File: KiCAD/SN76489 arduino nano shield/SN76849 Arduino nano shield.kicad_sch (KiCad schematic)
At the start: 14 parts, among them J1 Arduino_in, J2 audio_debug, J3 OLED_wit, J5 LOGO, J6 gat1, J7 gat2, J8 geluid_uit, U1 PCF8574, U3 SN76489, X1 CLK_DIP14_4Mhz

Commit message: Bijgewerkt naar KiCAD 7.0
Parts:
- U1, U3: footprint w_pth_circuits:dil_16-300_socket -> Package_DIP:DIP-16_W7.62mm
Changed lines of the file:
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@@
     (effects (font (size 1.1176 1.1176)) (justify left bottom))
   )
-  (label "VSS" (at 112.268 66.04 0)
+  (label "VSS" (at 112.268 66.04 0) (fields_autoplaced)
     (effects (font (size 0.9144 0.9144)) (justify left bottom))
   )
-  (label "P1" (at 181.61 40.894 0)
+  (label "P1" (at 181.61 40.894 0) (fields_autoplaced)
     (effects (font (size 0.8128 0.8128)) (justify left bottom))
   )
-  (label "VCC" (at 115.57 27.178 90)
+  (label "VCC" (at 115.57 27.178 90) (fields_autoplaced)
     (effects (font (size 0.9144 0.9144)) (justify left bottom))
   )
-  (label "VCC" (at 181.356 28.194 0)
+  (label "VCC" (at 181.356 28.194 0) (fields_autoplaced)
     (effects (font (size 0.7112 0.7112)) (justify left bottom))
   )
-  (label "SDA" (at 146.304 65.786 0)
+  (label "SDA" (at 146.304 65.786 0) (fields_autoplaced)
     (effects (font (size 0.7112 0.7112)) (justify left bottom))
   )
-  (label "SDA" (at 93.98 37.592 0)
+  (label "SDA" (at 93.98 37.592 0) (fields_autoplaced)
     (effects (font (size 0.7112 0.7112)) (justify left bottom))
   )
-  (label "VSS" (at 208.534 113.792 180)
+  (label "VSS" (at 208.534 113.792 180) (fields_autoplaced)
     (effects (font (size 0.9144 0.9144)) (justify right bottom))
   )
-  (label "P3" (at 129.794 42.672 0)
+  (label "P3" (at 129.794 42.672 0) (fields_autoplaced)
     (effects (font (size 0.9144 0.9144)) (justify left bottom))
   )
-  (label "CE" (at 148.59 40.894 0)
+  (label "CE" (at 148.59 40.894 0) (fields_autoplaced)
     (effects (font (size 0.9144 0.9144)) (justify left bottom))
   )
-  (label "VSS" (at 80.772 78.486 0)
+  (label "VSS" (at 80.772 78.486 0) (fields_autoplaced)
     (effects (font (size 0.7112 0.7112)) (justify left bottom))
   )
-  (label "P0" (at 129.794 35.052 0)
+  (label "P0" (at 129.794 35.052 0) (fields_autoplaced)
     (effects (font (size 0.9144 0.9144)) (justify left bottom))
   )
-  (label "P6" (at 148.59 30.734 0)
+  (label "P6" (at 148.59 30.734 0) (fields_autoplaced)
     (effects (font (size 0.8128 0.8128)) (justify left bottom))
   )
-  (label "P2" (at 129.794 40.132 0)
+  (label "P2" (at 129.794 40.132 0) (fields_autoplaced)
     (effects (font (size 0.9144 0.9144)) (justify left bottom))
   )
-  (label "P7" (at 148.59 33.274 0)
+  (label "P7" (at 148.59 33.274 0) (fields_autoplaced)
     (effects (font (size 0.8128 0.8128)) (justify left bottom))
   )
-  (label "Clock" (at 80.264 67.818 0)
+  (label "Clock" (at 80.264 67.818 0) (fields_autoplaced)
     (effects (font (size 0.8128 0.8128)) (justify left bottom))
   )
-  (label "VSS" (at 146.05 79.248 180)
+  (label "VSS" (at 146.05 79.248 180) (fields_autoplaced)
     (effects (font (size 0.9144 0.9144)) (justify right bottom))
   )
-  (label "~{WE}" (at 148.59 38.354 0)
+  (label "~{WE}" (at 148.59 38.354 0) (fields_autoplaced)
     (effects (font (size 0.8128 0.8128)) (justify left bottom))
   )
-  (label "P4" (at 129.794 45.212 0)
+  (label "P4" (at 129.794 45.212 0) (fields_autoplaced)
     (effects (font (size 0.9144 0.9144)) (justify left bottom))
   )
-  (label "~{WE}" (at 80.772 51.054 0)
+  (label "~{WE}" (at 80.772 51.054 0) (fields_autoplaced)
     (effects (font (size 0.8128 0.8128)) (justify left bottom))
   )
-  (label "Clock" (at 181.61 33.274 0)
+  (label "Clock" (at 181.61 33.274 0) (fields_autoplaced)
     (effects (font (size 0.9144 0.9144)) (justify left bottom))
   )
-  (label "P4" (at 181.61 30.734 0)
+  (label "P4" (at 181.61 30.734 0) (fields_autoplaced)
     (effects (font (size 0.9144 0.9144)) (justify left bottom))
   )
-  (label "P0" (at 181.61 43.434 0)
+  (label "P0" (at 181.61 43.434 0) (fields_autoplaced)
     (effects (font (size 0.8128 0.8128)) (justify left bottom))
   )
-  (label "P5" (at 129.794 47.752 0)
+  (label "P5" (at 129.794 47.752 0) (fields_autoplaced)
     (effects (font (size 0.9144 0.9144)) (justify left bottom))
   )
-  (label "SDA" (at 80.772 48.514 0)
+  (label "SDA" (at 80.772 48.514 0) (fields_autoplaced)
     (effects (font (size 0.7112 0.7112)) (justify left bottom))
   )
-  (label "P1" (at 129.54 37.592 0)
+  (label "P1" (at 129.54 37.592 0) (fields_autoplaced)
     (effects (font (size 0.9144 0.9144)) (justify left bottom))
   )
-  (label "P2" (at 181.61 38.354 0)
+  (label "P2" (at 181.61 38.354 0) (fields_autoplaced)
     (effects (font (size 0.8128 0.8128)) (justify left bottom))
   )
-  (label "P6" (at 129.794 50.292 0)
+  (label "P6" (at 129.794 50.292 0) (fields_autoplaced)
     (effects (font (size 0.9144 0.9144)) (justify left bottom))
   )
-  (label "VSS" (at 148.59 45.974 0)
+  (label "VSS" (at 148.59 45.974 0) (fields_autoplaced)
     (effects (font (size 0.9144 0.9144)) (justify left bottom))
   )
-  (label "SCL" (at 94.234 35.052 0)
+  (label "SCL" (at 94.234 35.052 0) (fields_autoplaced)
     (effects (font (size 0.7112 0.7112)) (justify left bottom))
   )
-  (label "Audio" (at 146.812 94.996 180)
+  (label "Audio" (at 146.812 94.996 180) (fields_autoplaced)
     (effects (font (size 0.9144 0.9144)) (justify right bottom))
   )
-  (label "P7" (at 129.794 52.832 0)
+  (label "P7" (at 129.794 52.832 0) (fields_autoplaced)
     (effects (font (size 0.9144 0.9144)) (justify left bottom))
   )
-  (label "SCL" (at 80.772 45.974 0)
+  (label "SCL" (at 80.772 45.974 0) (fields_autoplaced)
     (effects (font (size 0.7112 0.7112)) (justify left bottom))
   )
-  (label "SCL" (at 146.304 63.246 0)
+  (label "SCL" (at 146.304 63.246 0) (fields_autoplaced)
     (effects (font (size 0.7112 0.7112)) (justify left bottom))
   )
-  (label "P3" (at 181.61 35.814 0)
+  (label "P3" (at 181.61 35.814 0) (fields_autoplaced)
     (effects (font (size 0.8128 0.8128)) (justify left bottom))
   )
-  (label "VSS" (at 146.304 58.166 0)
+  (label "VSS" (at 146.304 58.166 0) (fields_autoplaced)
     (effects (font (size 0.7112 0.7112)) (justify left bottom))
   )
-  (label "VCC" (at 146.304 60.706 0)
+  (label "VCC" (at 146.304 60.706 0) (fields_autoplaced)
     (effects (font (size 0.7112 0.7112)) (justify left bottom))
   )
-  (label "P5" (at 148.59 28.194 0)
+  (label "P5" (at 148.59 28.194 0) (fields_autoplaced)
     (effects (font (size 0.8128 0.8128)) (justify left bottom))
   )
-  (label "VCC" (at 80.264 58.674 0)
+  (label "VCC" (at 80.264 58.674 0) (fields_autoplaced)
     (effects (font (size 0.7112 0.7112)) (justify left bottom))
   )
-  (label "Audio" (at 148.59 43.434 0)
+  (label "Audio" (at 148.59 43.434 0) (fields_autoplaced)
     (effects (font (size 0.9144 0.9144)) (justify left bottom))
   )
-  (label "VCC" (at 80.772 43.434 0)
+  (label "VCC" (at 80.772 43.434 0) (fields_autoplaced)
     (effects (font (size 0.7112 0.7112)) (justify left bottom))
   )
-  (label "VSS" (at 80.518 40.894 0)
+  (label "VSS" (at 80.518 40.894 0) (fields_autoplaced)
     (effects (font (size 0.7112 0.7112)) (justify left bottom))
   )
@@
       (effects (font (size 1.27 1.27)) (justify left))
     )
-    (property "Footprint" "w_pth_circuits:dil_16-300_socket" (at 115.57 45.212 0)
+    (property "Footprint" "Package_DIP:DIP-16_W7.62mm" (at 115.57 45.212 0)
       (effects (font (size 1.27 1.27)) hide)
     )
@@
       (effects (font (size 1.524 1.524)))
     )
-    (property "Footprint" "w_pth_circuits:dil_16-300_socket" (at 167.64 44.704 0)
+    (property "Footprint" "Package_DIP:DIP-16_W7.62mm" (at 167.64 44.704 0)
       (effects (font (size 1.524 1.524)) hide)
     )

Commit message: Bijgewerkt naar KiCAD 7.0
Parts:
- J1: footprint Pin_Headers:Pin_Header_Angled_1x05_Pitch2.54mm -> Connector_PinHeader_2.54mm:PinHeader_1x05_P2.54mm_Horizontal
- J2: footprint Pin_Headers:Pin_Header_Angled_1x03_Pitch2.54mm -> Connector_PinHeader_2.54mm:PinHeader_1x03_P2.54mm_Vertical
- J3: footprint Pin_Headers:Pin_Header_Angled_1x04_Pitch2.54mm -> Connector_PinHeader_2.54mm:PinHeader_1x04_P2.54mm_Horizontal
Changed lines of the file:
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@@
       (effects (font (size 0.762 0.762)))
     )
-    (property "Footprint" "Pin_Headers:Pin_Header_Angled_1x04_Pitch2.54mm" (at 155.448 60.706 0)
+    (property "Footprint" "Connector_PinHeader_2.54mm:PinHeader_1x04_P2.54mm_Horizontal" (at 155.448 60.706 0)
       (effects (font (size 1.27 1.27)) hide)
     )
@@
       (effects (font (size 0.762 0.762)))
     )
-    (property "Footprint" "Pin_Headers:Pin_Header_Angled_1x03_Pitch2.54mm" (at 137.922 112.522 0)
+    (property "Footprint" "Connector_PinHeader_2.54mm:PinHeader_1x03_P2.54mm_Vertical" (at 137.922 112.522 0)
       (effects (font (size 1.27 1.27)) hide)
     )
@@
       (effects (font (size 0.9652 0.9652)))
     )
-    (property "Footprint" "Pin_Headers:Pin_Header_Angled_1x05_Pitch2.54mm" (at 71.12 45.974 0)
+    (property "Footprint" "Connector_PinHeader_2.54mm:PinHeader_1x05_P2.54mm_Horizontal" (at 71.12 45.974 0)
       (effects (font (size 1.27 1.27)) hide)
     )

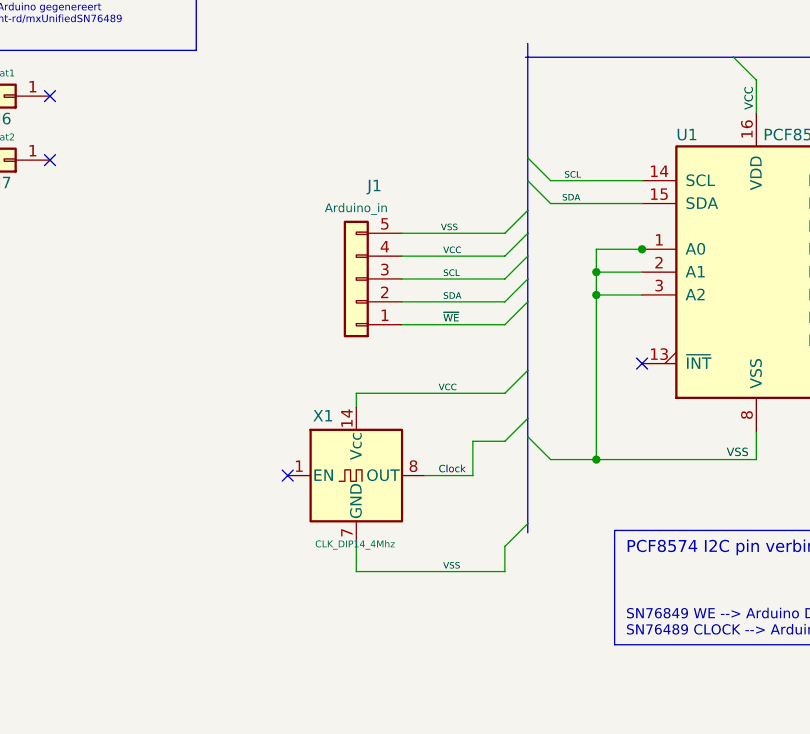
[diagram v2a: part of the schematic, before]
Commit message: Bijgewerkt naar KiCAD 7.0
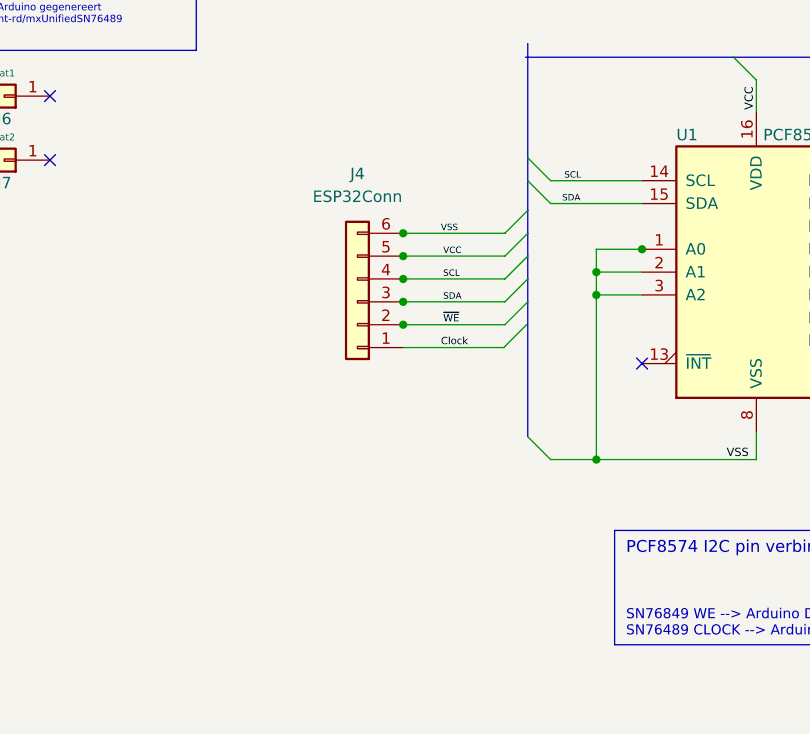
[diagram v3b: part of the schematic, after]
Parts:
- removed J1: Arduino_in, Connector_PinHeader_2.54mm:PinHeader_1x05_P2.54mm_Horizontal, symbol SN76849 Arduino nano shield-rescue:Conn_01x05-conn
- removed X1: CLK_DIP14_4Mhz, Oscillators:Oscillator_DIP-14_LargePads, symbol Oscillator:CXO_DIP14
- added J4: ESP32Conn, symbol Connector_Generic:Conn_01x06
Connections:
- net Clock: now also J4.1 (Pin_1)
- net GND: now also J4.6 (Pin_6)
- net SCL: now also J4.4 (Pin_4)
- net SDA: now also J4.3 (Pin_3)
- net VCC: now also J4.5 (Pin_5)
- net ~{WE}: now also J4.2 (Pin_2)
- no-connect marks 8 -> 7
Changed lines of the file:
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@@
   (junction (at 145.542 109.982) (diameter 0) (color 0 0 0 0)
   )
+  (junction (at 76.327 43.434) (diameter 0) (color 0 0 0 0)
+  )
+  (junction (at 76.327 48.514) (diameter 0) (color 0 0 0 0)
+  )
   (junction (at 184.912 130.048) (diameter 0) (color 0 0 0 0)
   )
@@
   (junction (at 137.16 23.876) (diameter 0) (color 0 0 0 0)
   )
+  (junction (at 76.327 40.894) (diameter 0) (color 0 0 0 0)
+  )
   (junction (at 184.912 111.506) (diameter 0) (color 0 0 0 0)
   )
@@
   (junction (at 151.13 115.062) (diameter 0) (color 0 0 0 0)
   )
+  (junction (at 76.327 45.974) (diameter 0) (color 0 0 0 0)
+  )
   (junction (at 97.79 47.752) (diameter 0) (color 0 0 0 0)
   )
@@
   )
   (junction (at 97.79 66.04) (diameter 0) (color 0 0 0 0)
+  )
+  (junction (at 76.327 51.054) (diameter 0) (color 0 0 0 0)
   )
   (no_connect (at 190.246 115.316))
@@
   (no_connect (at 180.34 45.974))
   (no_connect (at 37.084 25.654))
-  (no_connect (at 63.5 67.818))
   (no_connect (at 102.87 55.372))
   (bus_entry (at 87.63 40.894) (size 2.54 -2.54)
@@
     (stroke (width 0) (type default))
   )
-  (bus_entry (at 87.63 58.674) (size 2.54 -2.54)
-    (stroke (width 0) (type default))
-  )
   (bus_entry (at 139.7 45.974) (size 2.54 -2.54)
     (stroke (width 0) (type default))
   )
-  (bus_entry (at 87.63 64.008) (size 2.54 -2.54)
+  (bus_entry (at 87.503 53.594) (size 2.54 -2.54)
     (stroke (width 0) (type default))
   )
@@
     (stroke (width 0) (type default))
   )
-  (bus_entry (at 87.63 75.692) (size 2.54 -2.54)
-    (stroke (width 0) (type default))
-  )
   (bus_entry (at 113.03 21.336) (size 2.54 2.54)
     (stroke (width 0) (type default))
@@
     (stroke (width 0) (type default))
   )
-  (wire (pts (xy 87.63 64.008) (xy 84.074 64.008))
-    (stroke (width 0) (type default))
-  )
-  (wire (pts (xy 71.12 78.486) (xy 87.63 78.486))
-    (stroke (width 0) (type default))
-  )
   (bus (pts (xy 139.7 30.734) (xy 139.7 33.274))
     (stroke (width 0) (type default))
@@
     (stroke (width 0) (type default))
   )
-  (wire (pts (xy 76.2 40.894) (xy 87.63 40.894))
+  (wire (pts (xy 76.2 40.894) (xy 76.327 40.894))
     (stroke (width 0) (type default))
   )
@@
     (stroke (width 0) (type default))
   )
-  (bus (pts (xy 90.17 73.152) (xy 90.17 74.168))
-    (stroke (width 0) (type default))
-  )
   (wire (pts (xy 143.51 40.894) (xy 153.67 40.894))
     (stroke (width 0) (type default))
   )
+  (wire (pts (xy 76.327 40.894) (xy 87.63 40.894))
+    (stroke (width 0) (type default))
+  )
   (bus (pts (xy 137.16 45.212) (xy 137.16 47.752))
     (stroke (width 0) (type default))
@@
     (stroke (width 0) (type default))
   )
+  (wire (pts (xy 76.327 43.434) (xy 76.2 43.434))
+    (stroke (width 0) (type default))
+  )
   (bus (pts (xy 90.17 43.434) (xy 90.17 45.974))
     (stroke (width 0) (type default))
   )
-  (wire (pts (xy 71.12 58.674) (xy 71.12 60.198))
-    (stroke (width 0) (type default))
-  )
   (bus (pts (xy 139.7 55.626) (xy 139.7 58.166))
     (stroke (width 0) (type default))
   )
+  (wire (pts (xy 76.327 45.974) (xy 87.63 45.974))
+    (stroke (width 0) (type default))
+  )
   (wire (pts (xy 134.62 45.212) (xy 128.27 45.212))
     (stroke (width 0) (type default))
@@
     (stroke (width 0) (type default))
   )
-  (wire (pts (xy 71.12 75.438) (xy 71.12 78.486))
-    (stroke (width 0) (type default))
-  )
   (wire (pts (xy 97.79 47.752) (xy 102.87 47.752))
     (stroke (width 0) (type default))
   )
+  (wire (pts (xy 76.327 53.594) (xy 87.503 53.594))
+    (stroke (width 0) (type default))
+  )
   (wire (pts (xy 143.51 45.974) (xy 145.796 45.974))
     (stroke (width 0) (type default))
@@
     (stroke (width 0) (type default))
   )
-  (wire (pts (xy 76.2 45.974) (xy 87.63 45.974))
+  (wire (pts (xy 76.2 45.974) (xy 76.327 45.974))
     (stroke (width 0) (type default))
   )
@@
     (stroke (width 0) (type default))
   )
+  (wire (pts (xy 76.327 48.514) (xy 76.2 48.514))
+    (stroke (width 0) (type default))
+  )
   (bus (pts (xy 137.16 16.51) (xy 139.7 19.05))
     (stroke (width 0) (type default))
@@
     (stroke (width 0) (type default))
   )
-  (wire (pts (xy 87.63 78.486) (xy 87.63 75.692))
-    (stroke (width 0) (type default))
-  )
   (bus (pts (xy 139.7 48.514) (xy 139.7 55.626))
     (stroke (width 0) (type default))
@@
     (stroke (width 0) (type default))
   )
-  (wire (pts (xy 87.63 43.434) (xy 76.2 43.434))
+  (wire (pts (xy 87.63 43.434) (xy 76.327 43.434))
     (stroke (width 0) (type default))
   )
@@
     (stroke (width 0) (type default))
   )
-  (bus (pts (xy 90.17 56.134) (xy 90.17 61.468))
-    (stroke (width 0) (type default))
-  )
-  (bus (pts (xy 90.17 63.5) (xy 90.17 73.152))
+  (bus (pts (xy 90.17 48.514) (xy 90.17 63.5))
     (stroke (width 0) (type default))
   )
@@
     (stroke (width 0) (type default))
   )
-  (wire (pts (xy 84.074 64.008) (xy 84.074 67.818))
-    (stroke (width 0) (type default))
-  )
-  (wire (pts (xy 78.74 67.818) (xy 84.074 67.818))
-    (stroke (width 0) (type default))
-  )
   (wire (pts (xy 200.66 118.872) (xy 200.66 121.412))
     (stroke (width 0) (type default))
@@
     (stroke (width 0) (type default))
   )
-  (wire (pts (xy 87.63 58.674) (xy 71.12 58.674))
-    (stroke (width 0) (type default))
-  )
   (bus (pts (xy 139.7 92.456) (xy 139.7 100.076))
     (stroke (width 0) (type default))
@@
     (stroke (width 0) (type default))
   )
+  (wire (pts (xy 76.327 51.054) (xy 87.63 51.054))
+    (stroke (width 0) (type default))
+  )
   (wire (pts (xy 145.796 45.974) (xy 145.796 49.784))
     (stroke (width 0) (type default))
@@
     (stroke (width 0) (type default))
   )
-  (bus (pts (xy 90.17 61.468) (xy 90.17 63.5))
-    (stroke (width 0) (type default))
-  )
   (bus (pts (xy 90.17 32.512) (xy 90.17 35.052))
     (stroke (width 0) (type default))
@@
     (stroke (width 0) (type default))
   )
-  (wire (pts (xy 76.2 51.054) (xy 87.63 51.054))
+  (wire (pts (xy 76.2 51.054) (xy 76.327 51.054))
     (stroke (width 0) (type default))
   )
@@
     (stroke (width 0) (type default))
   )
-  (bus (pts (xy 90.17 48.514) (xy 90.17 56.134))
-    (stroke (width 0) (type default))
-  )
   (wire (pts (xy 150.368 60.706) (xy 142.24 60.706))
     (stroke (width 0) (type default))
@@
     (stroke (width 0) (type default))
   )
-  (wire (pts (xy 87.63 48.514) (xy 76.2 48.514))
+  (wire (pts (xy 87.63 48.514) (xy 76.327 48.514))
     (stroke (width 0) (type default))
   )
@@
     (effects (font (size 0.9144 0.9144)) (justify left bottom))
   )
-  (label "VSS" (at 80.772 78.486 0) (fields_autoplaced)
-    (effects (font (size 0.7112 0.7112)) (justify left bottom))
-  )
   (label "P0" (at 129.794 35.052 0) (fields_autoplaced)
     (effects (font (size 0.9144 0.9144)) (justify left bottom))
@@
     (effects (font (size 0.8128 0.8128)) (justify left bottom))
   )
-  (label "Clock" (at 80.264 67.818 0) (fields_autoplaced)
+  (label "Clock" (at 80.518 53.594 0) (fields_autoplaced)
     (effects (font (size 0.8128 0.8128)) (justify left bottom))
   )
@@
   (label "P5" (at 148.59 28.194 0) (fields_autoplaced)
     (effects (font (size 0.8128 0.8128)) (justify left bottom))
-  )
-  (label "VCC" (at 80.264 58.674 0) (fields_autoplaced)
-    (effects (font (size 0.7112 0.7112)) (justify left bottom))
   )
   (label "Audio" (at 148.59 43.434 0) (fields_autoplaced)
@@
     )
   )
-  (symbol (lib_id "Oscillator:CXO_DIP14") (at 71.12 67.818 0) (unit 1)
-    (in_bom yes) (on_board yes) (dnp no)
-    (property "Reference" "X1" (at 66.294 61.214 0)
-      (effects (font (size 1.27 1.27)) (justify left))
-    )
-    (property "Value" "CLK_DIP14_4Mhz" (at 66.548 75.438 0)
-      (effects (font (size 0.762 0.762)) (justify left))
-    )
-    (property "Footprint" "Oscillators:Oscillator_DIP-14_LargePads" (at 82.55 76.708 0)
-      (effects (font (size 1.27 1.27)) hide)
-    )
-    (property "Datasheet" "http://cdn-reichelt.de/documents/datenblatt/B400/OSZI.pdf" (at 68.58 67.818 0)
-      (effects (font (size 1.27 1.27)) hide)
-    )
-    (pin "1")
-    (pin "14")
-    (pin "7")
-    (pin "8")
-    (instances
-      (project "SN76849 Arduino nano shield"
-        (path "/d7982c1c-a003-41c6-88cd-de79c22de844"
-          (reference "X1") (unit 1)
-        )
-      )
-    )
-  )
-  (symbol (lib_id "SN76849 Arduino nano shield-rescue:Conn_01x05-conn") (at 71.12 45.974 180) (unit 1)
-    (in_bom yes) (on_board yes) (dnp no)
-    (property "Reference" "J1" (at 73.152 35.6362 0)
-      (effects (font (size 1.27 1.27)))
-    )
-    (property "Value" "Arduino_in" (at 71.12 38.1 0)
-      (effects (font (size 0.9652 0.9652)))
-    )
-    (property "Footprint" "Connector_PinHeader_2.54mm:PinHeader_1x05_P2.54mm_Horizontal" (at 71.12 45.974 0)
-      (effects (font (size 1.27 1.27)) hide)
-    )
-    (property "Datasheet" "~" (at 71.12 45.974 0)
+  (symbol (lib_id "Connector_Generic:Conn_01x06") (at 71.247 48.514 180) (unit 1)
+    (in_bom yes) (on_board yes) (dnp no) (fields_autoplaced)
+    (property "Reference" "J4" (at 71.247 34.29 0)
+      (effects (font (size 1.27 1.27)))
+    )
+    (property "Value" "ESP32Conn" (at 71.247 36.83 0)
+      (effects (font (size 1.27 1.27)))
+    )
+    (property "Footprint" "" (at 71.247 48.514 0)
+      (effects (font (size 1.27 1.27)) hide)
+    )
+    (property "Datasheet" "~" (at 71.247 48.514 0)
       (effects (font (size 1.27 1.27)) hide)
     )
@@
     (pin "4")
     (pin "5")
-    (instances
-      (project "SN76849 Arduino nano shield"
-        (path "/d7982c1c-a003-41c6-88cd-de79c22de844"
-          (reference "J1") (unit 1)
-        )
-      )
+    (pin "6")
+    (instances
+      (project "SN76849 Arduino nano shield"
+        (path "/d7982c1c-a003-41c6-88cd-de79c22de844"
+          (reference "J4") (unit 1)
+        )
+      )
